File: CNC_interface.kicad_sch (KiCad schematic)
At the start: 23 parts, among them J1 Conn_01x04_Male, J10 Conn_01x08, J11 Conn_01x08, J12 Conn_01x08, J13 Conn_01x08, J14 Conn_01x03_Male, J15 Conn_01x03_Male, J16 Conn_01x03_Male, J17 Conn_01x08, J18 Conn_01x10, J19 USB_C_Receptacle, J2 Conn_01x04_Male, J3 Conn_01x04_Male, J5 Screw_Terminal_01x02, J6 Screw_Terminal_01x02, J8 Conn_01x08, J9 Conn_01x08, Q1 Q_NMOS_GDS

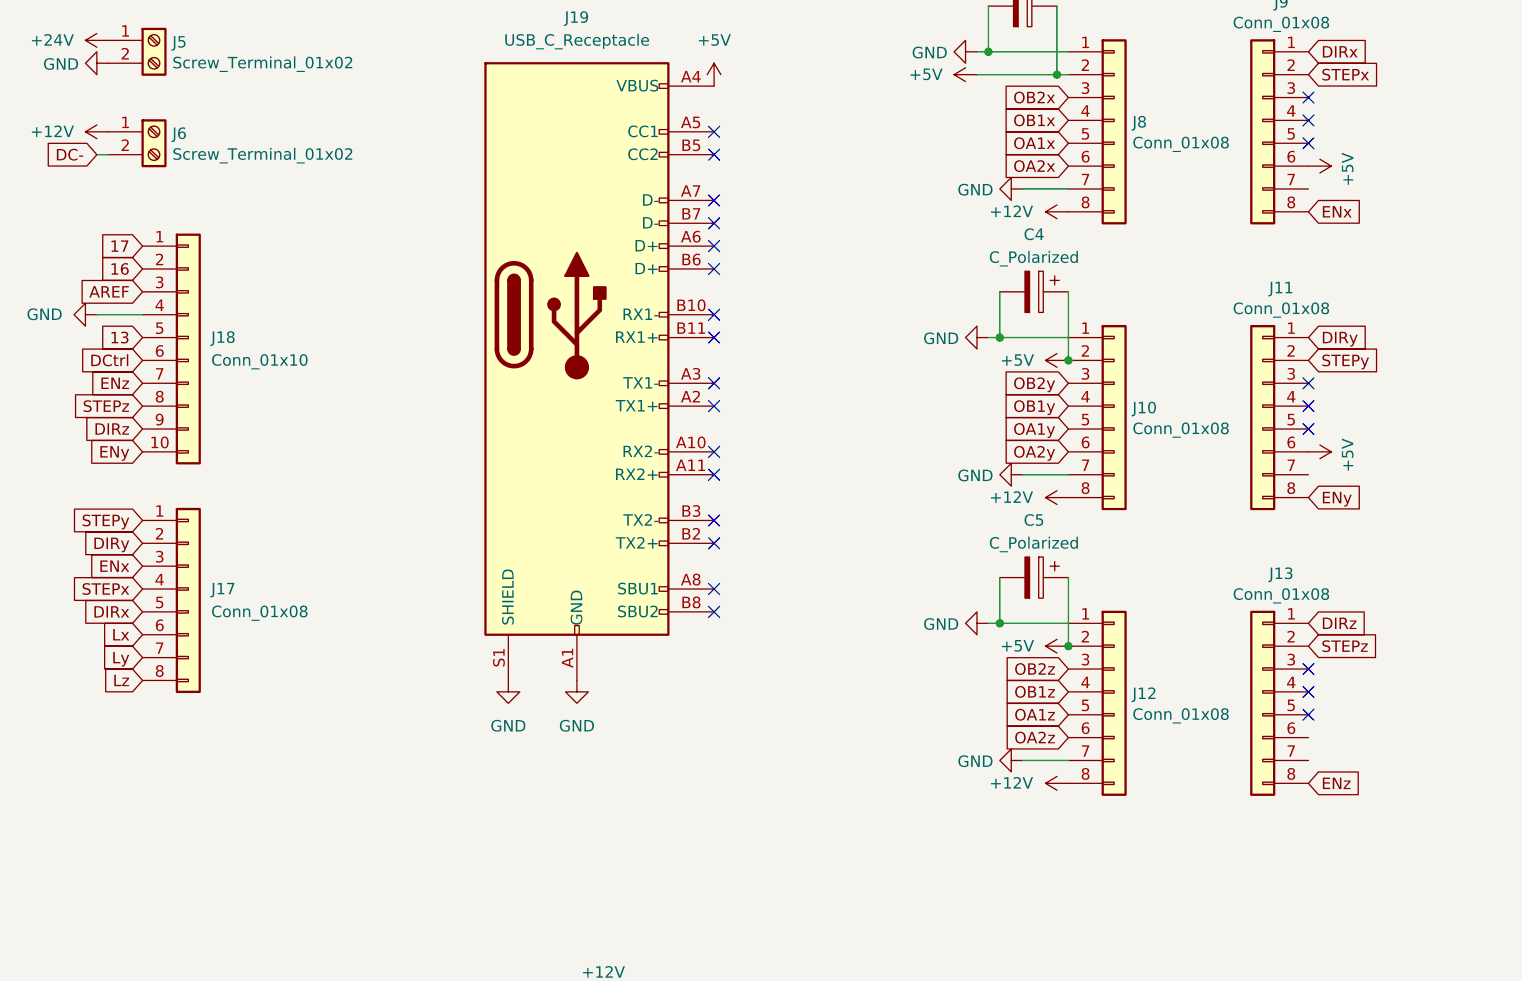
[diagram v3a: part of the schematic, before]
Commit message: Changing 12 to 24V
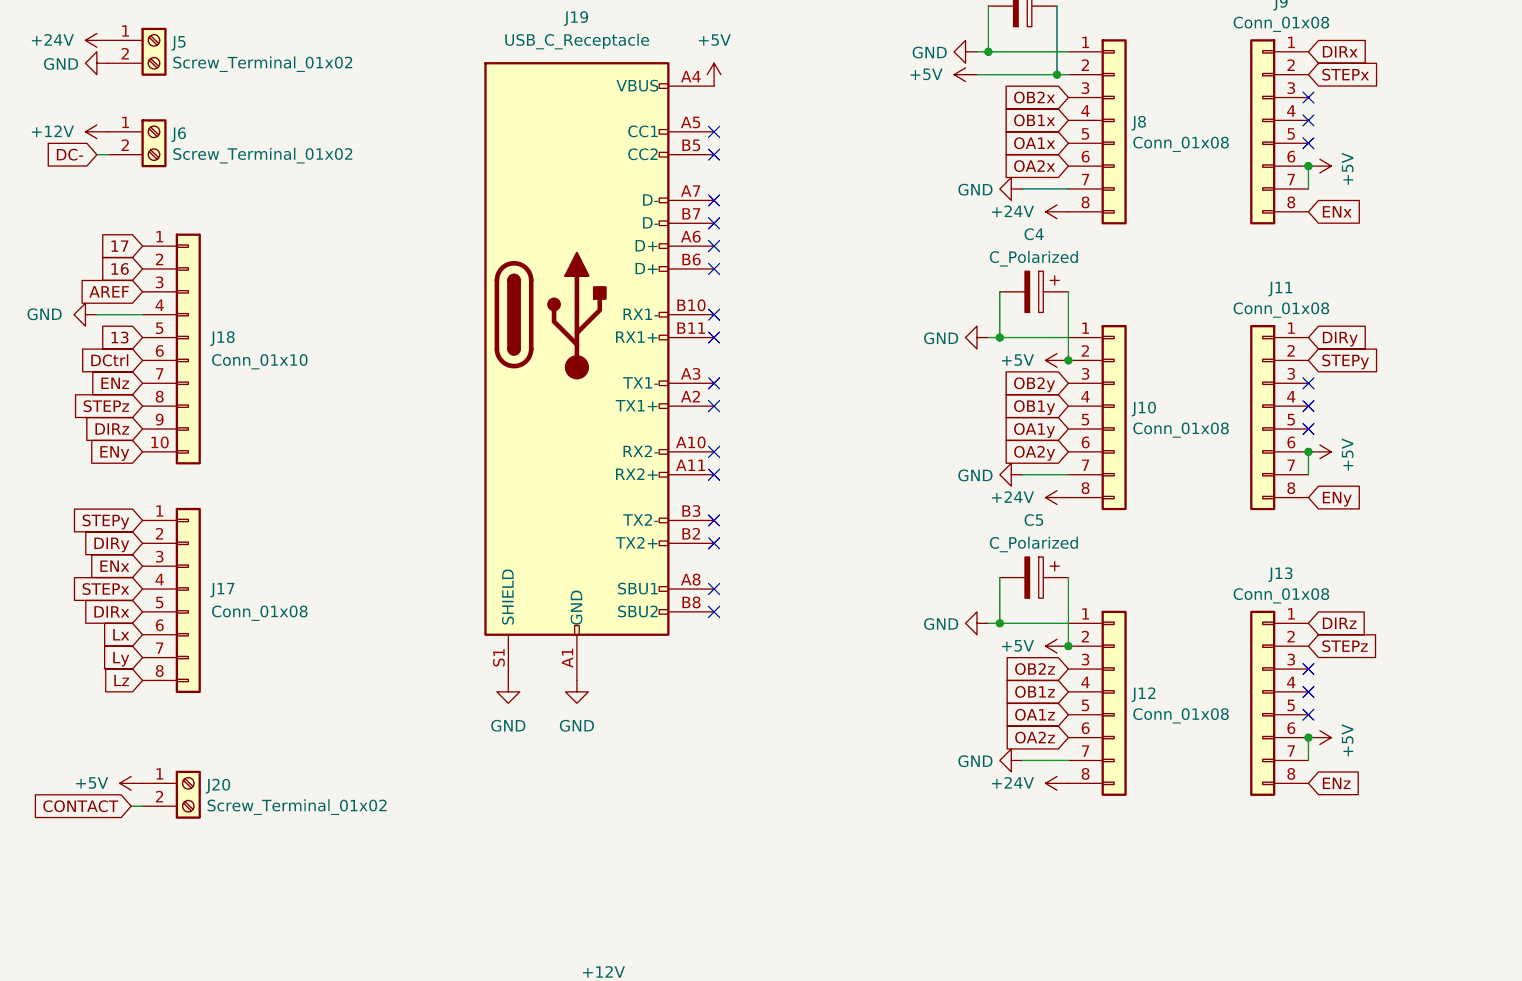
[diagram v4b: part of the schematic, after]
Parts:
- added J20: Screw_Terminal_01x02, CNC_interface:TerminalBlock_Phoenix_MKDSP-1,5-2-5.08_1x02_P5.08mm, symbol Connector:Screw_Terminal_01x02
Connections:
- net +12V: no longer J10.8 (Pin_8), J12.8 (Pin_8), J8.8 (Pin_8)
- net +24V: now also J10.8 (Pin_8), J12.8 (Pin_8), J8.8 (Pin_8)
- net +5V: now also J11.7 (Pin_7), J13.6 (Pin_6), J13.7 (Pin_7), J9.7 (Pin_7), J20.1 (Pin_1)
- new net CONTACT: J20.2 (Pin_2)

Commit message: add last footprints
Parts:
- added R2: 100k, Resistor_THT:R_Axial_DIN0207_L6.3mm_D2.5mm_P10.16mm_Horizontal, symbol Device:R
- C3, C4, C5: value C_Polarized -> 100uF; footprint (none) -> Capacitor_THT:CP_Radial_D6.3mm_P2.50mm
- R1: value R -> 100k; footprint (none) -> Resistor_THT:R_Axial_DIN0207_L6.3mm_D2.5mm_P10.16mm_Horizontal
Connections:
- net CONTACT is gone; now on net CONT: J20.2 (Pin_2)
- net GND: now also R2.2
- net 17 renamed CONT
- net CONT: now also R2.1

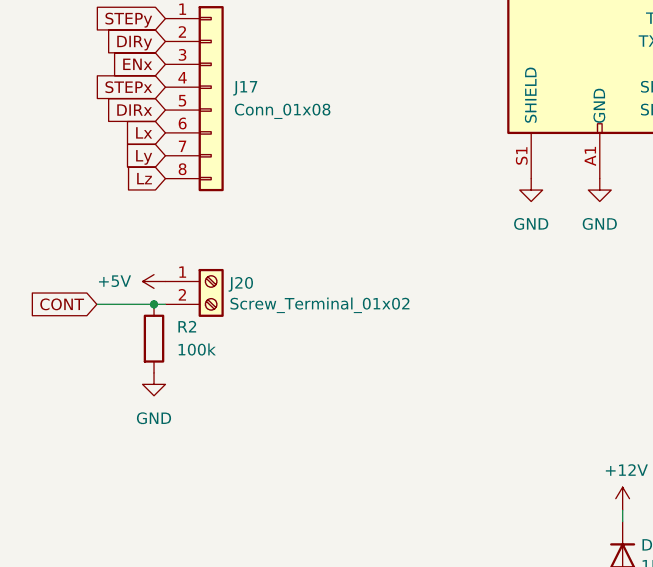
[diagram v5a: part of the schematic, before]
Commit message: update component names
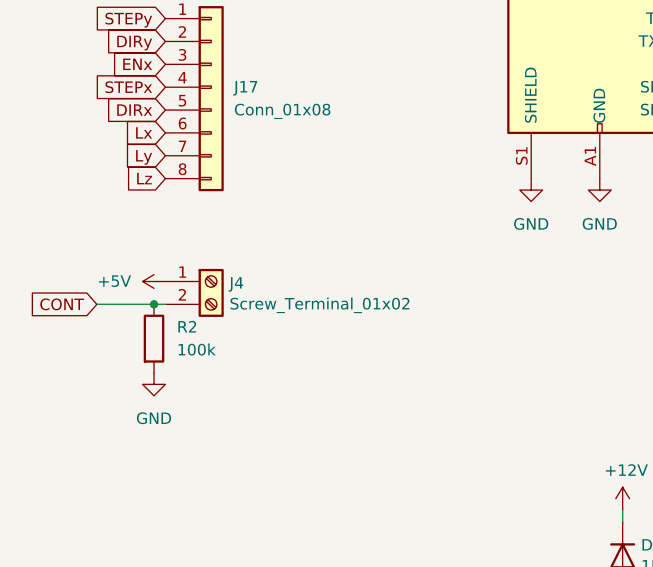
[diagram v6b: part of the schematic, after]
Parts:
- renumbered J20 to J4
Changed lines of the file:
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@@
   (symbol (lib_id "Connector:Screw_Terminal_01x02") (at 50.8 114.3 0) (unit 1)
     (in_bom yes) (on_board yes)
-    (property "Reference" "J20" (id 0) (at 52.832 114.5032 0)
+    (property "Reference" "J4" (id 0) (at 52.832 114.5032 0)
       (effects (font (size 1.27 1.27)) (justify left))
     )
@@
       (reference "J3") (unit 1) (value "Conn_01x04_Male") (footprint "Connector_JST:JST_XH_B4B-XH-A_1x04_P2.50mm_Vertical")
     )
+    (path "/f6130a08-de36-4d6d-b8cc-dfef4890d083"
+      (reference "J4") (unit 1) (value "Screw_Terminal_01x02") (footprint "CNC_interface:TerminalBlock_Phoenix_MKDSP-1,5-2-5.08_1x02_P5.08mm")
+    )
     (path "/00000000-0000-0000-0000-00006208728f"
       (reference "J5") (unit 1) (value "Screw_Terminal_01x02") (footprint "CNC_interface:TerminalBlock_Phoenix_MKDSP-1,5-2-5.08_1x02_P5.08mm")
@@
       (reference "J19") (unit 1) (value "USB_C_Receptacle") (footprint "Connector_USB:USB_C_Receptacle_Amphenol_12401548E4-2A_CircularHoles")
     )
-    (path "/f6130a08-de36-4d6d-b8cc-dfef4890d083"
-      (reference "J20") (unit 1) (value "Screw_Terminal_01x02") (footprint "CNC_interface:TerminalBlock_Phoenix_MKDSP-1,5-2-5.08_1x02_P5.08mm")
-    )
     (path "/8b7d305c-caee-4338-94fc-4790d784af7f/9264dc6e-5915-4d3e-9e3c-68b480f21536"
       (reference "L1") (unit 1) (value "10uH") (footprint "Inductor_SMD:L_TDK_SLF10145")
@@
     )
     (path "/8b7d305c-caee-4338-94fc-4790d784af7f/0e5d71c4-dc04-47da-990d-66c8f8e2e38b"
-      (reference "U4") (unit 1) (value "LM2596S-5") (footprint "Package_TO_SOT_SMD:TO-263-5_TabPin3")
+      (reference "U1") (unit 1) (value "LM2596S-5") (footprint "Package_TO_SOT_SMD:TO-263-5_TabPin3")
     )
     (path "/8b7d305c-caee-4338-94fc-4790d784af7f/5de2ac72-9f70-4078-8d15-4d73b7d95def"
-      (reference "U5") (unit 1) (value "LM2596S-12") (footprint "Package_TO_SOT_SMD:TO-263-5_TabPin3")
-    )
-  )
+      (reference "U2") (unit 1) (value "LM2596S-12") (footprint "Package_TO_SOT_SMD:TO-263-5_TabPin3")
+    )
+  )
